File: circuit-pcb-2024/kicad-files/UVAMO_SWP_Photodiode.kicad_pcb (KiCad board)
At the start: 2 copper layers, 40 x 50 mm, 33 parts, among them J1 Conn_01x02_Pin, J2 Conn_01x02_Pin, SW1 SW_Rotary_1x7_MP

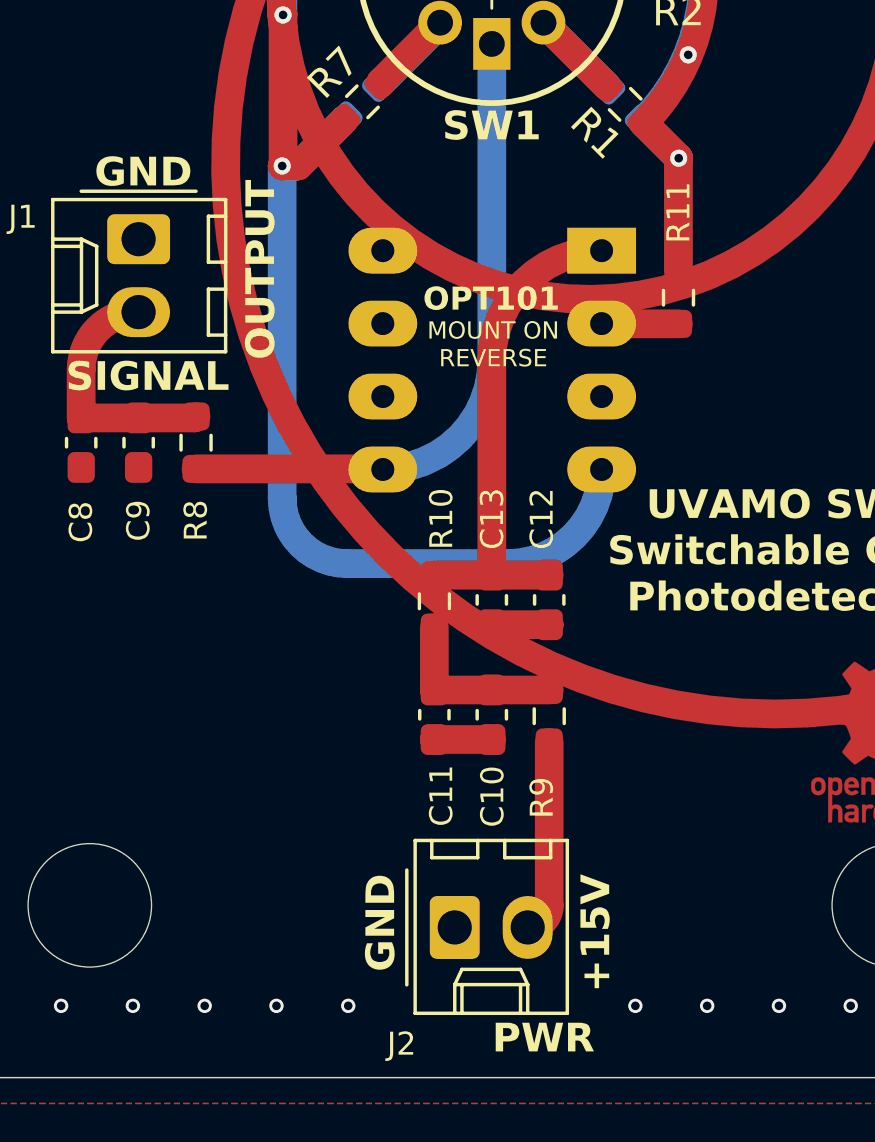
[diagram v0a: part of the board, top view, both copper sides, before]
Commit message: Updated PCB Files
Found issue in old PCB. Updated all related files
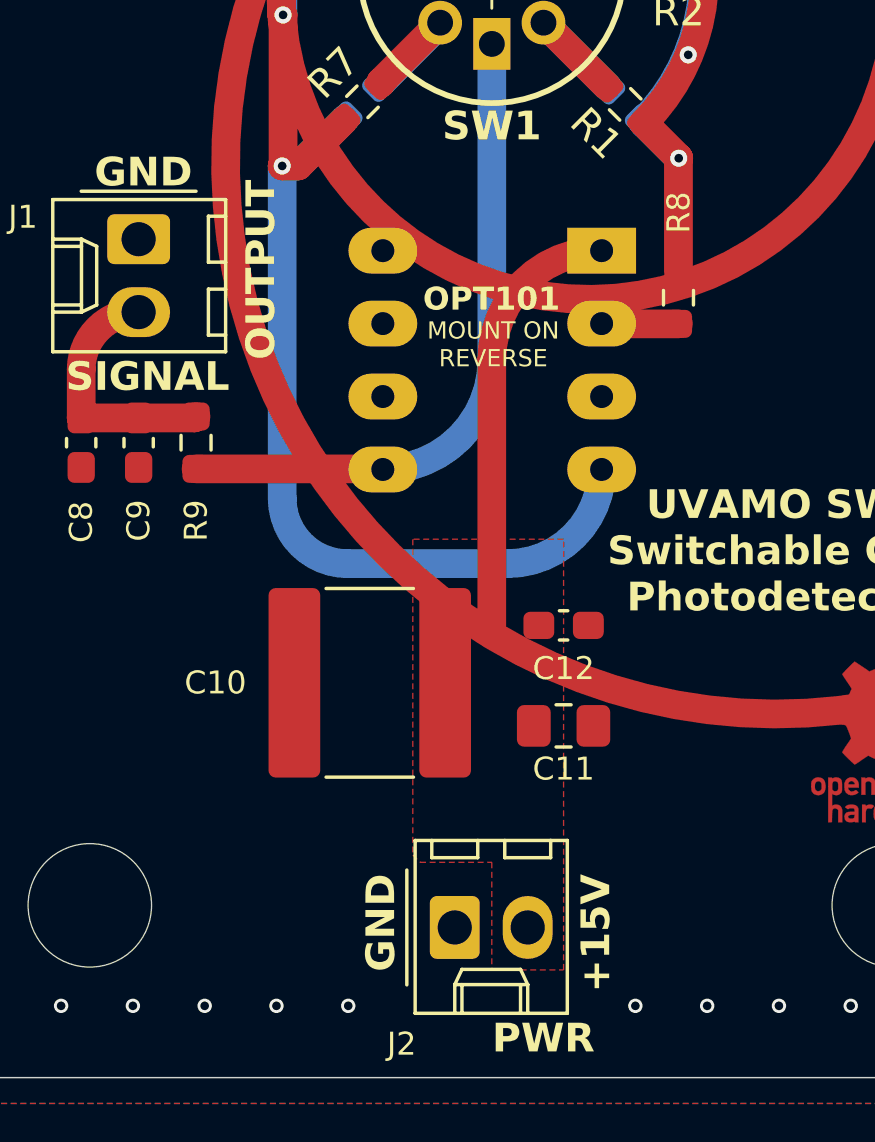
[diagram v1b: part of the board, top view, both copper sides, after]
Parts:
- removed C13: 100nF, Capacitor_SMD:C_0603_1608Metric_Pad1.08x0.95mm_HandSolder
- removed R10: 53k, Resistor_SMD:R_0603_1608Metric_Pad0.98x0.95mm_HandSolder
- removed the R9 at (157.0, 102.4)
- C10: value 100nF -> 1uF; footprint Capacitor_SMD:C_0603_1608Metric_Pad1.08x0.95mm_HandSolder -> Capacitor_SMD:C_2225_5664Metric_Pad1.80x6.60mm_HandSolder
- C11: footprint Capacitor_SMD:C_0603_1608Metric_Pad1.08x0.95mm_HandSolder -> Capacitor_SMD:C_0805_2012Metric_Pad1.18x1.45mm_HandSolder
- C12: value 100nF -> 10nF
- moved C11 4.52 mm to (157.5, 102.8), turned to 0 degrees
- moved C10 4.39 mm to (150.8, 101.2), turned to 180 degrees
- moved C12 1.02 mm to (157.5, 99.2), turned to 0 degrees
- renumbered R11 to R8, R8 to R9
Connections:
- C10 pad 1: Net-(C10-Pad1) -> VCC
- C11 pad 1: Net-(C10-Pad1) -> VCC
- J2 pad 2: Net-(J2-Pin_2) -> VCC
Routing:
- net Net-(J2-Pin_2): track 6.84 -> 0.00 mm
- net Net-(C10-Pad1): track 6.17 -> 0.00 mm
- net GND: track 4.00 -> 0.00 mm
- net VCC: track 17.3 -> 15.1 mm
- added copper zone on F.Cu, net VCC
